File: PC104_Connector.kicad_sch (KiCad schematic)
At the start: 2 parts

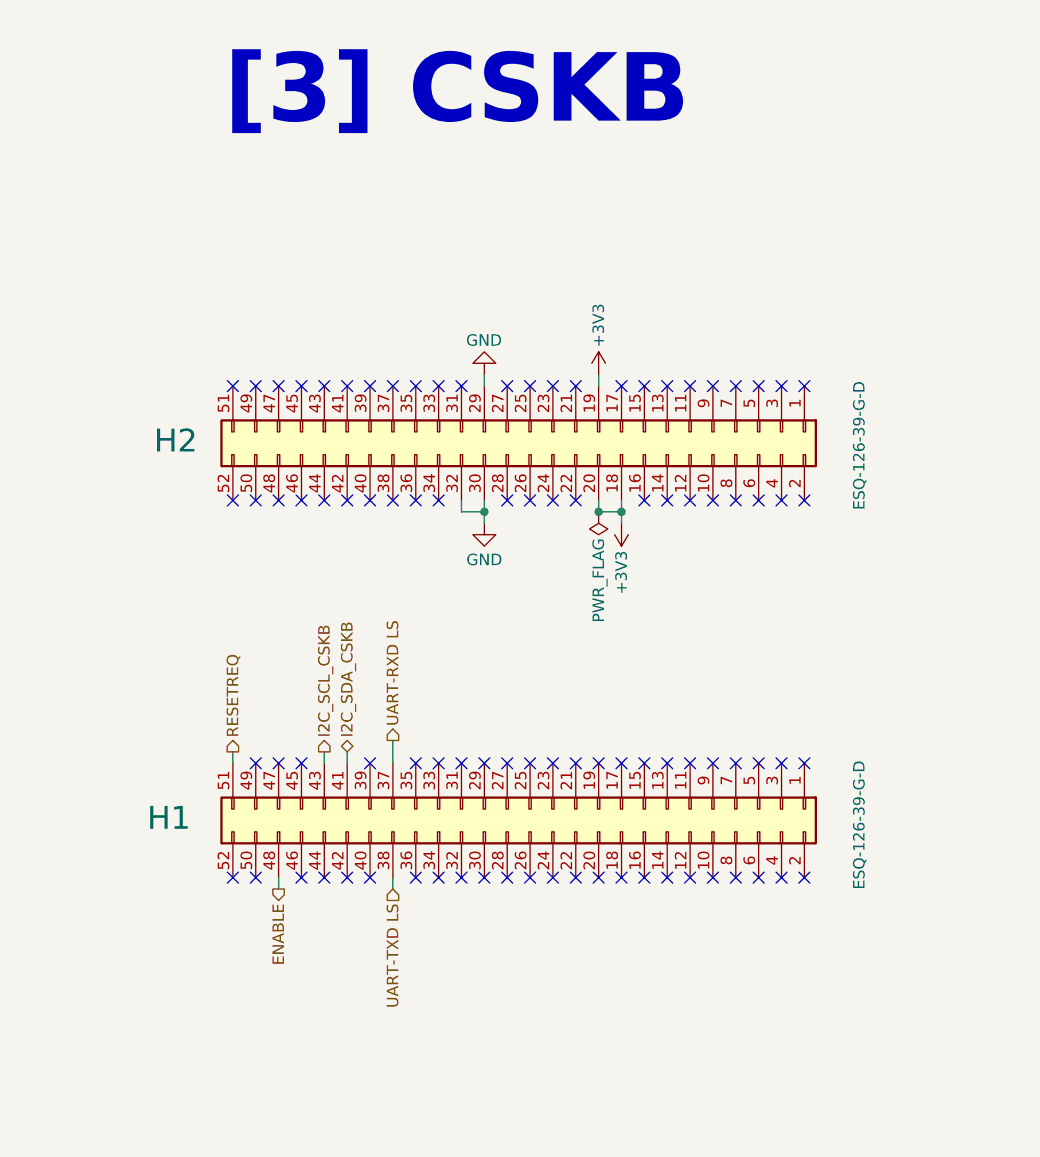
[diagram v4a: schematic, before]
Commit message: Changed connector orientation and power changes
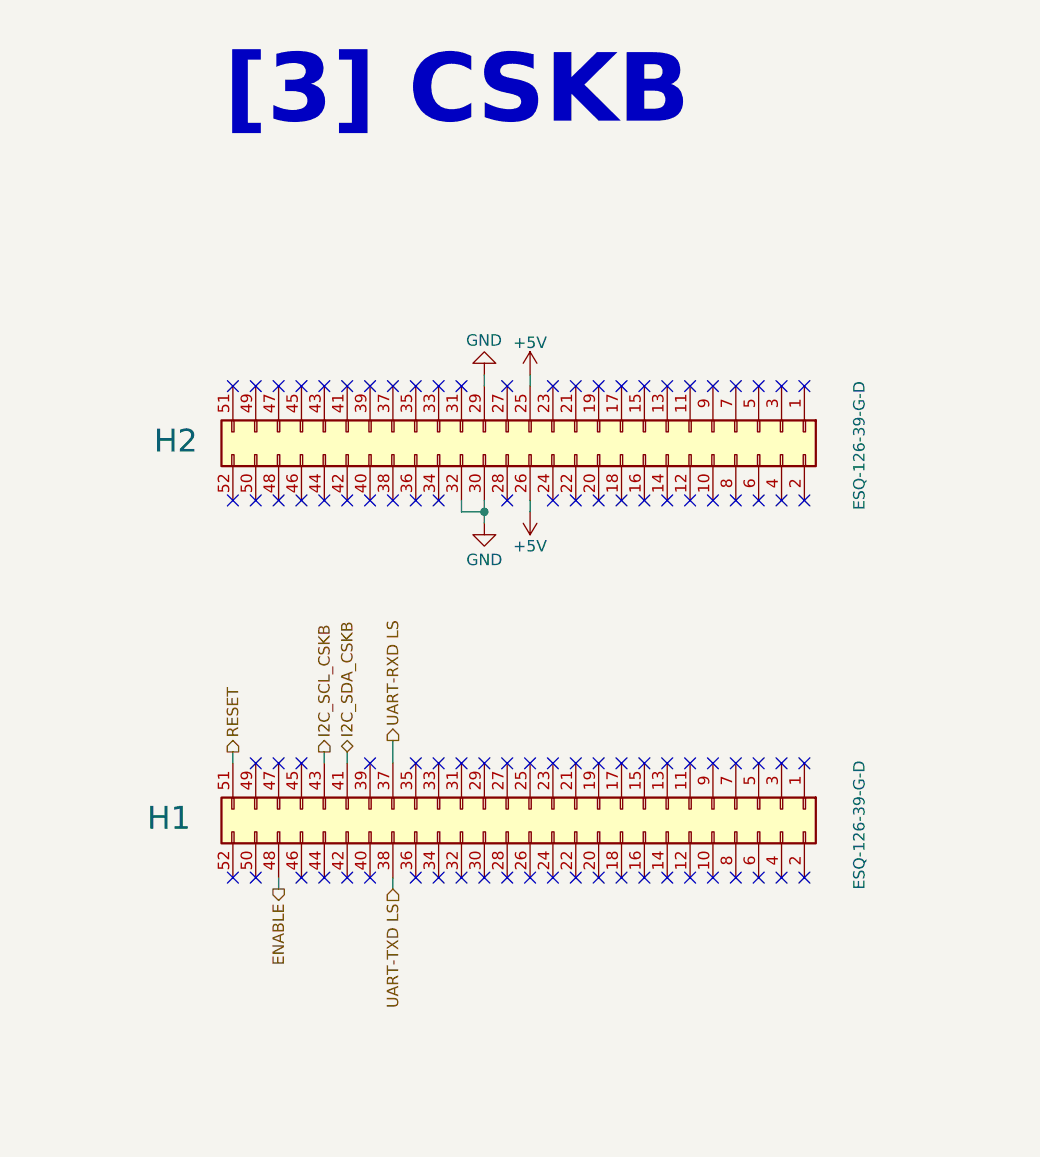
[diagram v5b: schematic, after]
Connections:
- net +5V: now reaches H2.25 (Pin_25)
- net +5V: now also H2.26 (Pin_26)
- removed net +3V3: H2.18 (Pin_18), H2.19 (Pin_19), H2.20 (Pin_20)
- net RESETREQ renamed RESET
- no-connect marks 92 -> 93
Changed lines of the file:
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@@
 		(color 0 0 0 0)
 	)
-	(junction
-		(at 162.56 72.39)
-		(diameter 0)
-		(color 0 0 0 0)
-	)
-	(junction
-		(at 160.02 72.39)
-		(diameter 0)
-		(color 0 0 0 0)
-	)
 	(no_connect
 		(at 142.24 58.42)
@@
 	)
 	(no_connect
-		(at 152.4 58.42)
-	)
-	(no_connect
 		(at 132.08 58.42)
 	)
@@
 	)
 	(no_connect
+		(at 160.02 58.42)
+	)
+	(no_connect
 		(at 162.56 58.42)
 	)
@@
 	)
 	(no_connect
+		(at 162.56 71.12)
+	)
+	(no_connect
 		(at 165.1 58.42)
 	)
@@
 	)
 	(no_connect
+		(at 160.02 71.12)
+	)
+	(no_connect
 		(at 134.62 58.42)
 	)
@@
 	)
 	(no_connect
-		(at 152.4 71.12)
-	)
-	(no_connect
 		(at 157.48 100.33)
 	)
@@
 	(wire
 		(pts
-			(xy 162.56 72.39) (xy 162.56 71.12)
-		)
-		(stroke
-			(width 0)
-			(type default)
-		)
-	)
-	(wire
-		(pts
 			(xy 144.78 72.39) (xy 144.78 71.12)
 		)
@@
 	(wire
 		(pts
-			(xy 160.02 72.39) (xy 160.02 71.12)
-		)
-		(stroke
-			(width 0)
-			(type default)
-		)
-	)
-	(wire
-		(pts
-			(xy 162.56 73.66) (xy 162.56 72.39)
+			(xy 152.4 72.39) (xy 152.4 71.12)
 		)
 		(stroke
@@
 	(wire
 		(pts
-			(xy 162.56 72.39) (xy 160.02 72.39)
-		)
-		(stroke
-			(width 0)
-			(type default)
-		)
-	)
-	(wire
-		(pts
 			(xy 124.46 114.3) (xy 124.46 113.03)
 		)
@@
 	(wire
 		(pts
-			(xy 160.02 57.15) (xy 160.02 58.42)
-		)
-		(stroke
-			(width 0)
-			(type default)
-		)
-	)
-	(wire
-		(pts
 			(xy 147.32 73.66) (xy 147.32 72.39)
 		)
@@
 		(pts
 			(xy 147.32 72.39) (xy 147.32 71.12)
+		)
+		(stroke
+			(width 0)
+			(type default)
+		)
+	)
+	(wire
+		(pts
+			(xy 152.4 57.15) (xy 152.4 58.42)
 		)
 		(stroke
@@
 		)
 	)
-	(hierarchical_label "RESETREQ"
+	(hierarchical_label "RESET"
 		(shape output)
 		(at 119.38 99.06 90)
@@
 	)
 	(symbol
-		(lib_id "power:+3V3")
-		(at 160.02 57.15 0)
-		(unit 1)
-		(body_style 1)
-		(exclude_from_sim no)
-		(in_bom yes)
-		(on_board yes)
-		(in_pos_files yes)
-		(dnp no)
-		(property "Reference" "#PWR04"
-			(at 160.02 60.96 0)
-			(hide yes)
-			(show_name no)
-			(do_not_autoplace no)
-			(effects
-				(font
-					(size 1.27 1.27)
-				)
-			)
-		)
-		(property "Value" "+3V3"
-			(at 160.02 54.102 90)
-			(show_name no)
-			(do_not_autoplace no)
-			(effects
-				(font
-					(size 1.27 1.27)
-				)
-				(justify left)
-			)
-		)
-		(property "Footprint" ""
-			(at 160.02 57.15 0)
-			(hide yes)
-			(show_name no)
-			(do_not_autoplace no)
-			(effects
-				(font
-					(size 1.27 1.27)
-				)
-			)
-		)
-		(property "Datasheet" ""
-			(at 160.02 57.15 0)
-			(hide yes)
-			(show_name no)
-			(do_not_autoplace no)
-			(effects
-				(font
-					(size 1.27 1.27)
-				)
-			)
-		)
-		(property "Description" "Power symbol creates a global label with name \"+3V3\""
-			(at 160.02 57.15 0)
-			(hide yes)
-			(show_name no)
-			(do_not_autoplace no)
-			(effects
-				(font
-					(size 1.27 1.27)
-				)
-			)
-		)
-		(pin "1"
-		)
-		(instances
-			(project "adapter-pcb"
-				(path "/94da9b83-1146-4f01-8e34-8153765b0257/6da06bd5-7839-43dd-9065-41aec0431e8e"
-					(reference "#PWR04")
-					(unit 1)
-				)
-			)
-		)
-	)
-	(symbol
-		(lib_id "power:+3V3")
-		(at 162.56 73.66 180)
+		(lib_id "power:+5V")
+		(at 152.4 57.15 0)
 		(unit 1)
 		(body_style 1)
@@
 		(dnp no)
 		(property "Reference" "#PWR03"
-			(at 162.56 69.85 0)
-			(hide yes)
-			(show_name no)
-			(do_not_autoplace no)
-			(effects
-				(font
-					(size 1.27 1.27)
-				)
-			)
-		)
-		(property "Value" "+3V3"
-			(at 162.56 76.708 90)
-			(show_name no)
-			(do_not_autoplace no)
-			(effects
-				(font
-					(size 1.27 1.27)
-				)
-				(justify left)
+			(at 152.4 60.96 0)
+			(hide yes)
+			(show_name no)
+			(do_not_autoplace no)
+			(effects
+				(font
+					(size 1.27 1.27)
+				)
+			)
+		)
+		(property "Value" "+5V"
+			(at 152.4 53.594 0)
+			(show_name no)
+			(do_not_autoplace no)
+			(effects
+				(font
+					(size 1.27 1.27)
+				)
 			)
 		)
 		(property "Footprint" ""
-			(at 162.56 73.66 0)
+			(at 152.4 57.15 0)
 			(hide yes)
 			(show_name no)
@@
 		)
 		(property "Datasheet" ""
-			(at 162.56 73.66 0)
-			(hide yes)
-			(show_name no)
-			(do_not_autoplace no)
-			(effects
-				(font
-					(size 1.27 1.27)
-				)
-			)
-		)
-		(property "Description" "Power symbol creates a global label with name \"+3V3\""
-			(at 162.56 73.66 0)
+			(at 152.4 57.15 0)
+			(hide yes)
+			(show_name no)
+			(do_not_autoplace no)
+			(effects
+				(font
+					(size 1.27 1.27)
+				)
+			)
+		)
+		(property "Description" "Power symbol creates a global label with name \"+5V\""
+			(at 152.4 57.15 0)
 			(hide yes)
 			(show_name no)
@@
 	)
 	(symbol
+		(lib_id "power:+5V")
+		(at 152.4 72.39 180)
+		(unit 1)
+		(body_style 1)
+		(exclude_from_sim no)
+		(in_bom yes)
+		(on_board yes)
+		(in_pos_files yes)
+		(dnp no)
+		(property "Reference" "#PWR04"
+			(at 152.4 68.58 0)
+			(hide yes)
+			(show_name no)
+			(do_not_autoplace no)
+			(effects
+				(font
+					(size 1.27 1.27)
+				)
+			)
+		)
+		(property "Value" "+5V"
+			(at 152.4 76.2 0)
+			(show_name no)
+			(do_not_autoplace no)
+			(effects
+				(font
+					(size 1.27 1.27)
+				)
+			)
+		)
+		(property "Footprint" ""
+			(at 152.4 72.39 0)
+			(hide yes)
+			(show_name no)
+			(do_not_autoplace no)
+			(effects
+				(font
+					(size 1.27 1.27)
+				)
+			)
+		)
+		(property "Datasheet" ""
+			(at 152.4 72.39 0)
+			(hide yes)
+			(show_name no)
+			(do_not_autoplace no)
+			(effects
+				(font
+					(size 1.27 1.27)
+				)
+			)
+		)
+		(property "Description" "Power symbol creates a global label with name \"+5V\""
+			(at 152.4 72.39 0)
+			(hide yes)
+			(show_name no)
+			(do_not_autoplace no)
+			(effects
+				(font
+					(size 1.27 1.27)
+				)
+			)
+		)
+		(pin "1"
+		)
+		(instances
+			(project "adapter-pcb"
+				(path "/94da9b83-1146-4f01-8e34-8153765b0257/6da06bd5-7839-43dd-9065-41aec0431e8e"
+					(reference "#PWR04")
+					(unit 1)
+				)
+			)
+		)
+	)
+	(symbol
 		(lib_id "Connector_Generic:Conn_02x26_Odd_Even")
 		(at 152.4 105.41 270)
@@
 					(unit 1)
 				)
-			)
-		)
-	)
-	(symbol
-		(lib_id "power:PWR_FLAG")
-		(at 160.02 72.39 180)
-		(unit 1)
-		(body_style 1)
-		(exclude_from_sim no)
-		(in_bom yes)
-		(on_board yes)
-		(in_pos_files yes)
-		(dnp no)
-		(property "Reference" "#FLG01"
-			(at 160.02 74.295 0)
-			(hide yes)
-			(show_name no)
-			(do_not_autoplace no)
-			(effects
-				(font
-					(size 1.27 1.27)
-				)
-			)
-		)
-		(property "Value" "PWR_FLAG"
-			(at 160.02 80.01 90)
-			(show_name no)
-			(do_not_autoplace no)
-			(effects
-				(font
-					(size 1.27 1.27)
-				)
-			)
-		)
-		(property "Footprint" ""
-			(at 160.02 72.39 0)
-			(hide yes)
-			(show_name no)
-			(do_not_autoplace no)
-			(effects
-				(font
-					(size 1.27 1.27)
-				)
-			)
-		)
-		(property "Datasheet" ""
-			(at 160.02 72.39 0)
-			(hide yes)
-			(show_name no)
-			(do_not_autoplace no)
-			(effects
-				(font
-					(size 1.27 1.27)
-				)
-			)
-		)
-		(property "Description" "Special symbol for telling ERC where power comes from"
-			(at 160.02 72.39 0)
-			(hide yes)
-			(show_name no)
-			(do_not_autoplace no)
-			(effects
-				(font
-					(size 1.27 1.27)
-				)
-			)
-		)
-		(pin "1"
-		)
-		(instances
-			(project "adapter-pcb"
-				(path "/94da9b83-1146-4f01-8e34-8153765b0257/6da06bd5-7839-43dd-9065-41aec0431e8e"
-					(reference "#FLG01")
-					(unit 1)
-				)

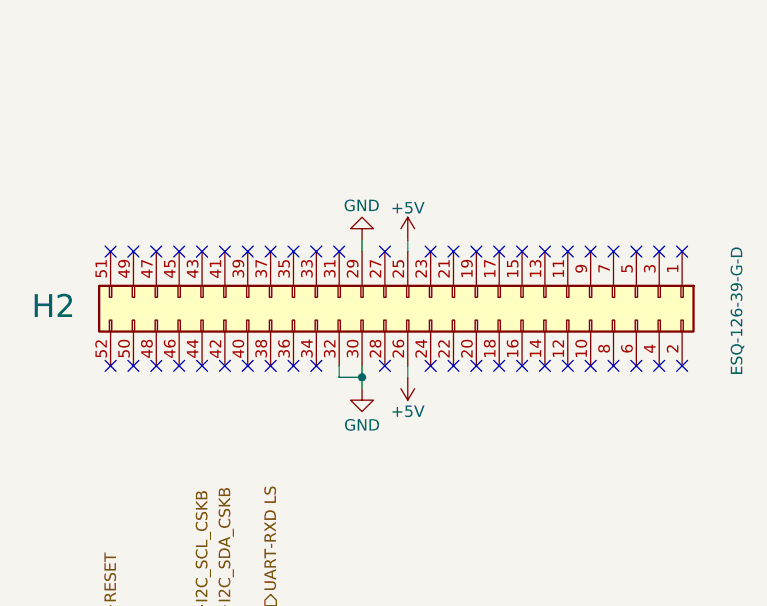
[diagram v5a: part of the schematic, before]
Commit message: added mroe GND pins and moved power to PDM lines
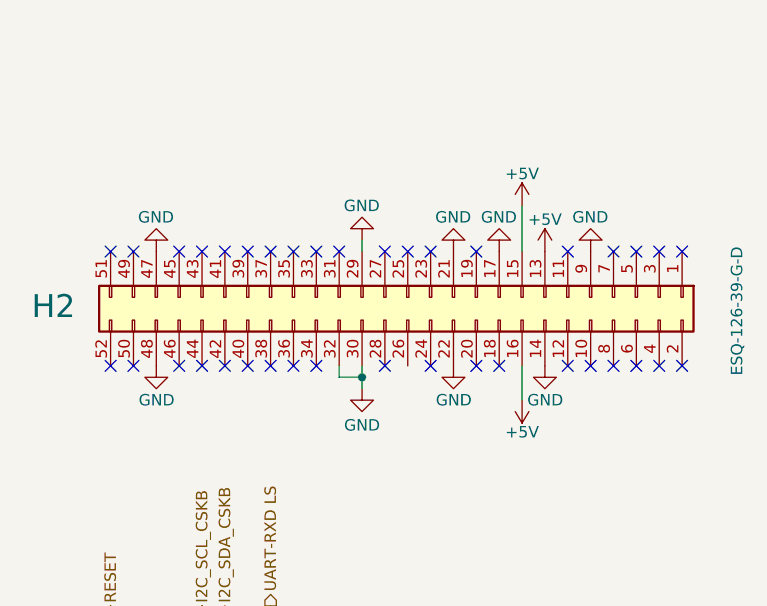
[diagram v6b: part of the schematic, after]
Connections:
- net +5V: now also H2.13 (Pin_13), H2.15 (Pin_15), H2.16 (Pin_16); no longer H2.25 (Pin_25), H2.26 (Pin_26)
- net GND: now also H2.14 (Pin_14), H2.17 (Pin_17), H2.21 (Pin_21), H2.22 (Pin_22), H2.47 (Pin_47), H2.48 (Pin_48), H2.9 (Pin_9)
- no-connect marks 93 -> 84

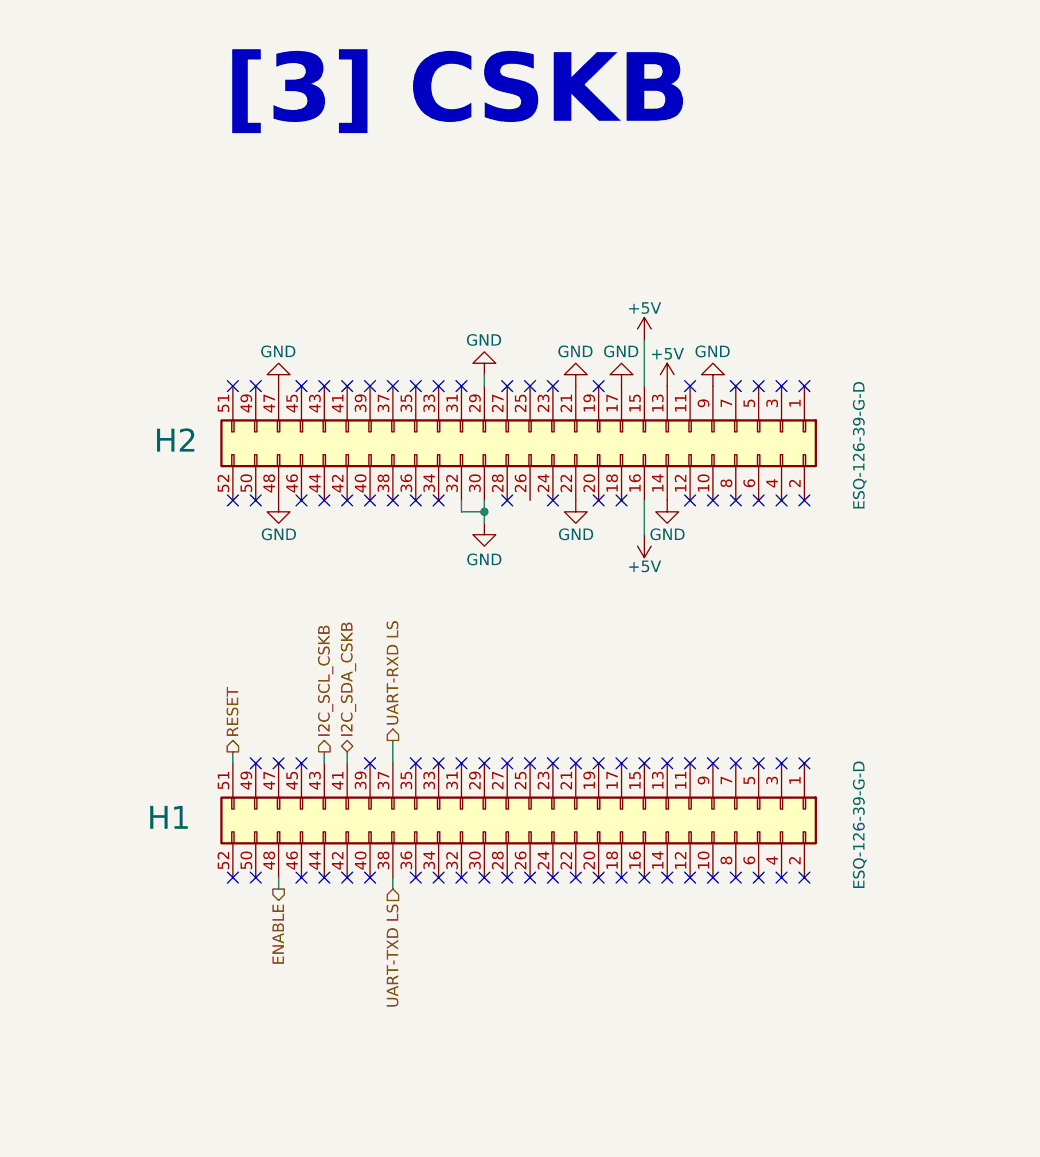
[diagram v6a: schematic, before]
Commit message: added solder bridges and updated BOM
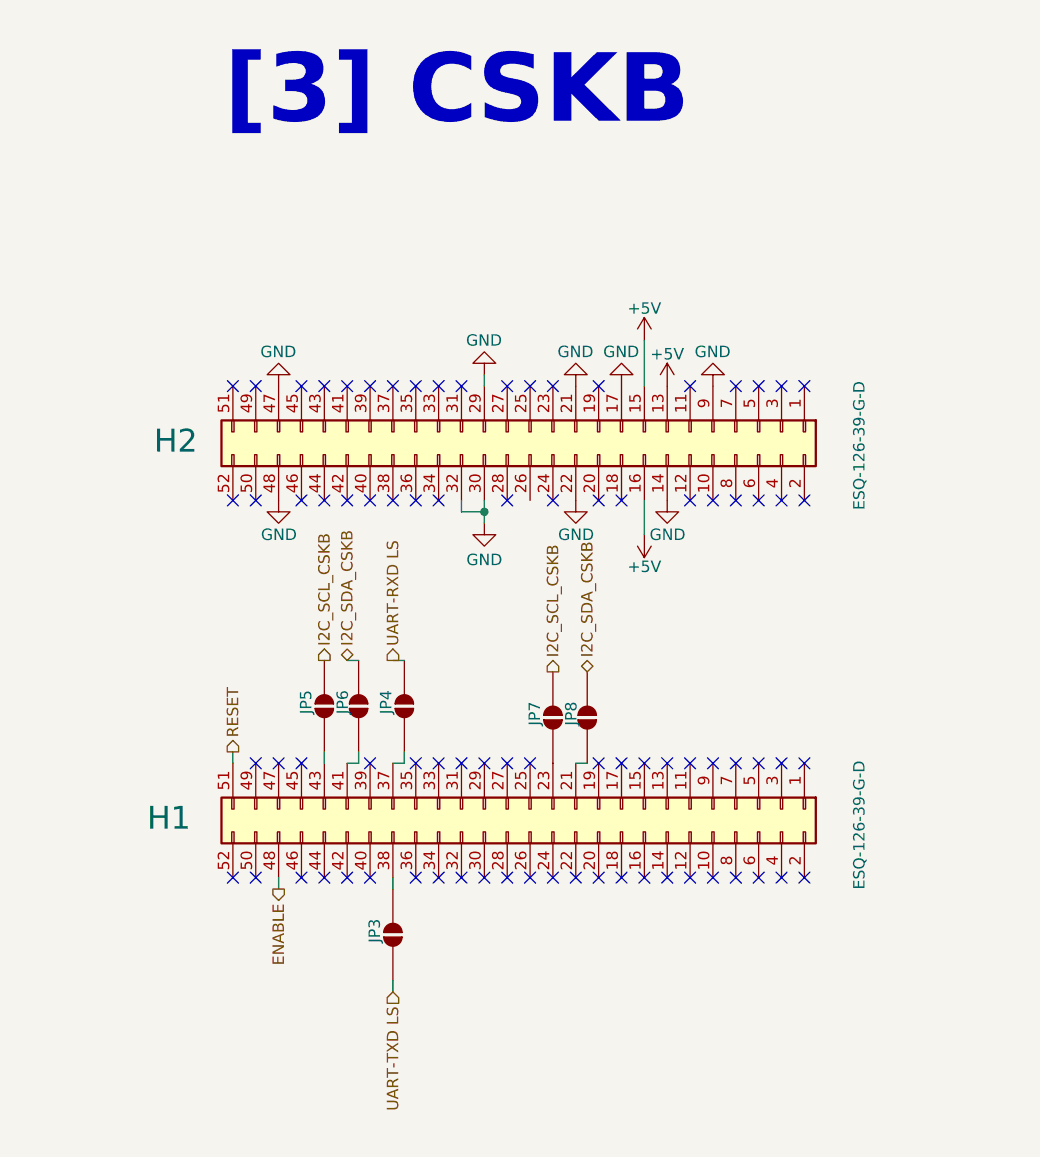
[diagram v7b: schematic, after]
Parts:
- added JP3, JP4: SolderJumper_2_Open, Jumper:SolderJumper-2_P1.3mm_Bridged_RoundedPad1.0x1.5mm, symbol Jumper:SolderJumper_2_Open
- added JP5, JP6, JP7, JP8: SolderJumper_2_Open, Jumper:SolderJumper-2_P1.3mm_Open_RoundedPad1.0x1.5mm, symbol Jumper:SolderJumper_2_Open
- H1, H2: External Part Num (none) -> C7466599; External Part Number ESQ-126-39-G-D -> (none); MPN C7466599 -> ESQ-126-39-G-D
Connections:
- net I2C_SCL_CSKB: now also JP5.2 (B), JP7.2 (B); no longer H1.43 (Pin_43)
- net I2C_SDA_CSKB: now also JP6.2 (B), JP8.2 (B); no longer H1.41 (Pin_41)
- net UART-RXD LS: now also JP4.2 (B); no longer H1.37 (Pin_37)
- net UART-TXD LS: now also JP3.1 (A); no longer H1.38 (Pin_38)
- net at H1.21 (Pin_21): now also JP8.1 (A)
- net at H1.23 (Pin_23): now also JP7.1 (A)
- new net: H1.41 (Pin_41), JP6.1 (A)
- new net: H1.43 (Pin_43), JP5.1 (A)
- new net: H1.37 (Pin_37), JP4.1 (A)
- new net: H1.38 (Pin_38), JP3.2 (B)
- no-connect marks 84 -> 82
